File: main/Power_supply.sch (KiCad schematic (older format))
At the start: 39 parts, among them IC1 TPS54294PWP, IC2 TPS54294PWP, J3 Barrel_Jack

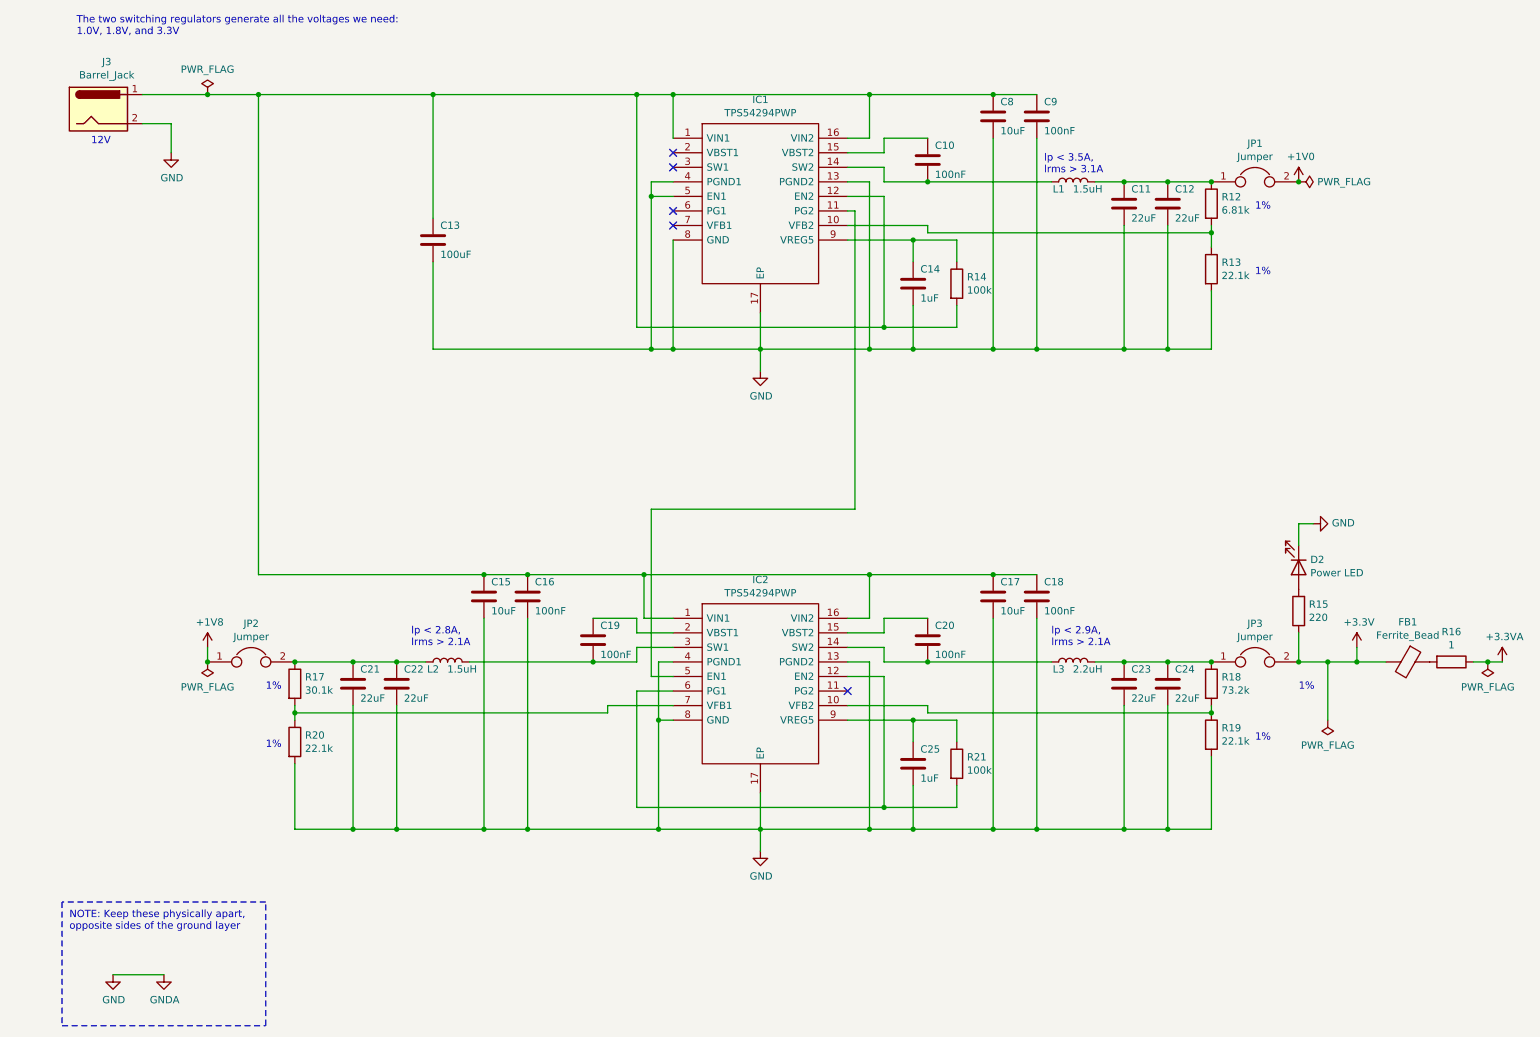
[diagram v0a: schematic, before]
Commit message: DAC: Remove amplifier, replace with low pass as per datasheet
Also: a lot of footprint association
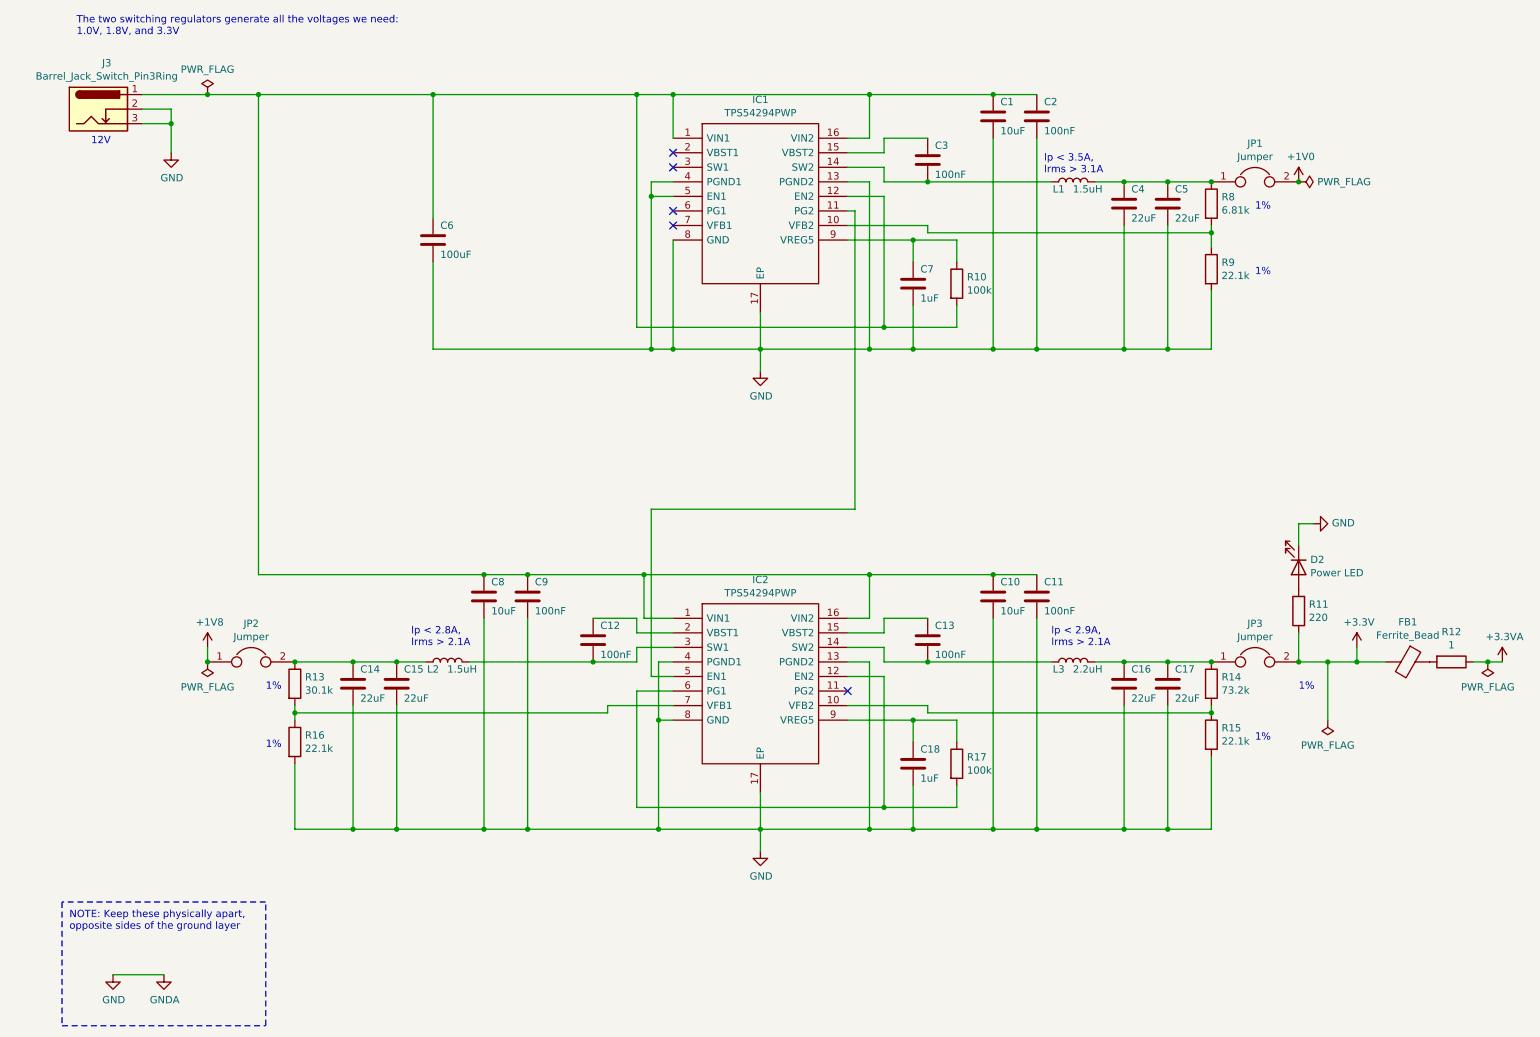
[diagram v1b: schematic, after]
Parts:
- removed J3: Barrel_Jack, symbol Connector:Barrel_Jack
- added J3: Barrel_Jack_Switch_Pin3Ring, Connector_BarrelJack:BarrelJack_CUI_PJ-102AH_Horizontal, symbol Connector:Barrel_Jack_Switch_Pin3Ring
- C1: renamed from C8; footprint (none) -> Capacitor_SMD:C_0805_2012Metric_Pad1.18x1.45mm_HandSolder
- C10: renamed from C17; footprint (none) -> Capacitor_SMD:C_0805_2012Metric_Pad1.18x1.45mm_HandSolder
- C11: renamed from C18; footprint (none) -> Capacitor_SMD:C_0805_2012Metric_Pad1.18x1.45mm_HandSolder
- C12: renamed from C19; footprint (none) -> Capacitor_SMD:C_0805_2012Metric_Pad1.18x1.45mm_HandSolder
- C13: renamed from C20; footprint (none) -> Capacitor_SMD:C_0805_2012Metric_Pad1.18x1.45mm_HandSolder
- C14: renamed from C21; footprint (none) -> Capacitor_SMD:C_0805_2012Metric_Pad1.18x1.45mm_HandSolder
- C15: renamed from C22; footprint (none) -> Capacitor_SMD:C_0805_2012Metric_Pad1.18x1.45mm_HandSolder
- C16: renamed from C23; footprint (none) -> Capacitor_SMD:C_0805_2012Metric_Pad1.18x1.45mm_HandSolder
- C17: renamed from C24; footprint (none) -> Capacitor_SMD:C_0805_2012Metric_Pad1.18x1.45mm_HandSolder
- C18: renamed from C25; footprint (none) -> Capacitor_SMD:C_0805_2012Metric_Pad1.18x1.45mm_HandSolder
- C2: renamed from C9; footprint (none) -> Capacitor_SMD:C_0805_2012Metric_Pad1.18x1.45mm_HandSolder
- C3: renamed from C10; footprint (none) -> Capacitor_SMD:C_0805_2012Metric_Pad1.18x1.45mm_HandSolder
- C4: renamed from C11; footprint (none) -> Capacitor_SMD:C_0805_2012Metric_Pad1.18x1.45mm_HandSolder
- C5: renamed from C12; footprint (none) -> Capacitor_SMD:C_0805_2012Metric_Pad1.18x1.45mm_HandSolder
- C7: renamed from C14; footprint (none) -> Capacitor_SMD:C_0805_2012Metric_Pad1.18x1.45mm_HandSolder
- C8: renamed from C15; footprint (none) -> Capacitor_SMD:C_0805_2012Metric_Pad1.18x1.45mm_HandSolder
- C9: renamed from C16; footprint (none) -> Capacitor_SMD:C_0805_2012Metric_Pad1.18x1.45mm_HandSolder
- FB1: footprint (none) -> Resistor_SMD:R_0805_2012Metric_Pad1.20x1.40mm_HandSolder
- JP1, JP2, JP3: footprint (none) -> Connector_PinHeader_2.54mm:PinHeader_2x01_P2.54mm_Vertical
- renumbered C13 to C6, R14 to R10, R15 to R11, R16 to R12, R17 to R13, R18 to R14, R19 to R15, R20 to R16, R21 to R17, R12 to R8, R13 to R9
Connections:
- net GND: now also J3.2, J3.3
- net at C1.1, C10.1, C11.1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: now also J3.1

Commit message: Start PCB layout
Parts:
- D2: Manufacturer_Name (none) -> Wurth Electronic; Manufacturer_Part_Number (none) -> 150080RS75000; URL (none) -> https://no.farnell.com/wurth-elektronik/150080rs75000/led-0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
- FB1: Manufacturer_Name (none) -> TE; Manufacturer_Part_Number (none) -> BMB2A0060LN2; URL (none) -> https://no.farnell.com/sigmainductors-te-connectivity/bmb2a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
- IC1, IC2: URL (none) -> https://no.farnell.com/texas-instruments/tps54294pwp/buck-s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
- J3: Manufacturer_Name (none) -> CUI Devices; Manufacturer_Part_Number (none) -> PJ-002A; URL (none) -> https://www.digikey.no/product-detail/no/cui-devices/PJ-002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
- L1, L2: Manufacturer_Name (none) -> muRata; Manufacturer_Part_Number (none) -> 1286AS-H-2R2M=P2; URL (none) -> https://no.farnell.com/murata/1286as-h-2r2m-p2/inductor-2-2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
- L3: Manufacturer_Name (none) -> muRata; Manufacturer_Part_Number (none) -> DFE201610E-1R5M=P2; URL (none) -> https://no.farnell.com/murata/dfe201610e-1r5m-p2/inductor-1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
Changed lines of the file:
@@
 F 10 "TPS54294PWP" H 5900 4200 50  0001 L CNN "Arrow Part Number"
 F 11 "https://www.arrow.com/en/products/tps54294pwp/texas-instruments" H 5900 4100 50  0001 L CNN "Arrow Price/Stock"
+F 12 "https://no.farnell.com/texas-instruments/tps54294pwp/buck-sync-adj-2a-dl-16htssop/dp/3008251" H 4850 4900 50  0001 C CNN "URL"
 	1    4850 4900
 	1    0    0    -1
@@
 F 1 "1.5uH" V 3250 5100 50  0000 C CNN
 F 2 "Inductor_SMD:L_1806_4516Metric_Pad1.57x1.80mm_HandSolder" H 3300 5200 50  0001 C CNN
-F 3 "~" H 3300 5200 50  0001 C CNN
+F 3 "https://www.farnell.com/datasheets/2021974.pdf" H 3300 5200 50  0001 C CNN
+F 4 "muRata" H 3300 5200 50  0001 C CNN "Manufacturer_Name"
+F 5 "1286AS-H-2R2M=P2" H 3300 5200 50  0001 C CNN "Manufacturer_Part_Number"
+F 6 "https://no.farnell.com/murata/1286as-h-2r2m-p2/inductor-2-2uh-20-1-5a-shld-0806/dp/2530046?st=inductor%20smd%200806" H 3300 5200 50  0001 C CNN "URL"
 	1    3300 5200
 	0    -1   -1   0
@@
 F 1 "2.2uH" V 7550 5100 50  0000 C CNN
 F 2 "Inductor_SMD:L_1806_4516Metric_Pad1.57x1.80mm_HandSolder" H 7600 5200 50  0001 C CNN
-F 3 "~" H 7600 5200 50  0001 C CNN
+F 3 "https://www.farnell.com/datasheets/2339713.pdf" H 7600 5200 50  0001 C CNN
+F 4 "muRata" H 7600 5200 50  0001 C CNN "Manufacturer_Name"
+F 5 "DFE201610E-1R5M=P2" H 7600 5200 50  0001 C CNN "Manufacturer_Part_Number"
+F 6 "https://no.farnell.com/murata/dfe201610e-1r5m-p2/inductor-1-5uh-2-4a-0806-shielded/dp/2776797?st=inductor%20smd%200806" H 7600 5200 50  0001 C CNN "URL"
 	1    7600 5200
 	0    -1   -1   0
@@
 F 1 "Ferrite_Bead" V 9717 5200 50  0000 C CNN
 F 2 "Resistor_SMD:R_0805_2012Metric_Pad1.20x1.40mm_HandSolder" V 9830 5200 50  0001 C CNN
-F 3 "~" H 9900 5200 50  0001 C CNN
+F 3 "https://www.farnell.com/datasheets/38013.pdf" H 9900 5200 50  0001 C CNN
+F 4 "TE" H 9900 5200 50  0001 C CNN "Manufacturer_Name"
+F 5 "BMB2A0060LN2" H 9900 5200 50  0001 C CNN "Manufacturer_Part_Number"
+F 6 "https://no.farnell.com/sigmainductors-te-connectivity/bmb2a0060ln2/ferrite-bead-0-05ohm-850ma-0805/dp/1193419?st=ferrite%20bead%200805" H 9900 5200 50  0001 C CNN "URL"
 	1    9900 5200
 	0    1    1    0
@@
 F 10 "TPS54294PWP" H 5900 900 50  0001 L CNN "Arrow Part Number"
 F 11 "https://www.arrow.com/en/products/tps54294pwp/texas-instruments" H 5900 800 50  0001 L CNN "Arrow Price/Stock"
+F 12 "https://no.farnell.com/texas-instruments/tps54294pwp/buck-sync-adj-2a-dl-16htssop/dp/3008251" H 4850 1600 50  0001 C CNN "URL"
 	1    4850 1600
 	1    0    0    -1
@@
 F 1 "1.5uH" V 7550 1800 50  0000 C CNN
 F 2 "Inductor_SMD:L_1806_4516Metric_Pad1.57x1.80mm_HandSolder" H 7600 1900 50  0001 C CNN
-F 3 "~" H 7600 1900 50  0001 C CNN
+F 3 "https://www.farnell.com/datasheets/2021974.pdf" H 7600 1900 50  0001 C CNN
+F 4 "muRata" H 7600 1900 50  0001 C CNN "Manufacturer_Name"
+F 5 "1286AS-H-2R2M=P2" H 7600 1900 50  0001 C CNN "Manufacturer_Part_Number"
+F 6 "https://no.farnell.com/murata/1286as-h-2r2m-p2/inductor-2-2uh-20-1-5a-shld-0806/dp/2530046?st=inductor%20smd%200806" H 7600 1900 50  0001 C CNN "URL"
 	1    7600 1900
 	0    -1   -1   0
@@
 F 1 "Power LED" V 9188 4630 50  0000 L CNN
 F 2 "LED_SMD:LED_0805_2012Metric_Pad1.15x1.40mm_HandSolder" H 9150 4550 50  0001 C CNN
-F 3 "~" H 9150 4550 50  0001 C CNN
+F 3 "https://www.farnell.com/datasheets/1911350.pdf" H 9150 4550 50  0001 C CNN
+F 4 "Wurth Electronic" H 9150 4550 50  0001 C CNN "Manufacturer_Name"
+F 5 "150080RS75000" H 9150 4550 50  0001 C CNN "Manufacturer_Part_Number"
+F 6 "https://no.farnell.com/wurth-elektronik/150080rs75000/led-0805-red-150mcd-625nm/dp/2322077?st=0805%20led" H 9150 4550 50  0001 C CNN "URL"
 	1    9150 4550
 	0    1    1    0
@@
 F 1 "Barrel_Jack_Switch_Pin3Ring" H 957 1626 50  0000 C CNN
 F 2 "Connector_BarrelJack:BarrelJack_CUI_PJ-102AH_Horizontal" H 950 1360 50  0001 C CNN
-F 3 "~" H 950 1360 50  0001 C CNN
+F 3 "https://www.cuidevices.com/product/resource/digikeypdf/pj-002a.pdf~" H 950 1360 50  0001 C CNN
+F 4 "CUI Devices" H 900 1400 50  0001 C CNN "Manufacturer_Name"
+F 5 " PJ-002A " H 900 1400 50  0001 C CNN "Manufacturer_Part_Number"
+F 6 "https://www.digikey.no/product-detail/no/cui-devices/PJ-002A/CP-002A-ND/96962" H 900 1400 50  0001 C CNN "URL"
 	1    900  1400
 	1    0    0    -1

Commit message: Continue PCB layout
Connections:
- net +1V8: now also JP2.2; no longer JP2.1
- net at C14.1, C15.1, L2.1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: now also JP2.1; no longer JP2.2
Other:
- moved on the sheet: JP2
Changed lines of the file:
@@
 U 1 1 6165E780
 P 1950 5200
-F 0 "JP2" H 1950 5464 50  0000 C CNN
-F 1 "Jumper" H 1950 5373 50  0000 C CNN
+F 0 "JP2" H 1950 5100 50  0000 C CNN
+F 1 "Jumper" H 1950 5000 50  0000 C CNN
 F 2 "Connector_PinHeader_2.54mm:PinHeader_2x01_P2.54mm_Vertical" H 1950 5200 50  0001 C CNN
 F 3 "~" H 1950 5200 50  0001 C CNN
 	1    1950 5200
-	1    0    0    -1
+	-1   0    0    1
 $EndComp
 Connection ~ 1650 5200

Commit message: Some more routing
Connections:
- net at C12.2, IC2.3 (SW1): now also L2.1; no longer L2.2
- net at C14.1, C15.1, JP2.1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: now also L2.2; no longer L2.1
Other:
- moved on the sheet: L2
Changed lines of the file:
@@
 F 6 "https://no.farnell.com/murata/1286as-h-2r2m-p2/inductor-2-2uh-20-1-5a-shld-0806/dp/2530046?st=inductor%20smd%200806" H 3300 5200 50  0001 C CNN "URL"
 	1    3300 5200
-	0    -1   -1   0
+	0    1    1    0
 $EndComp
 $Comp

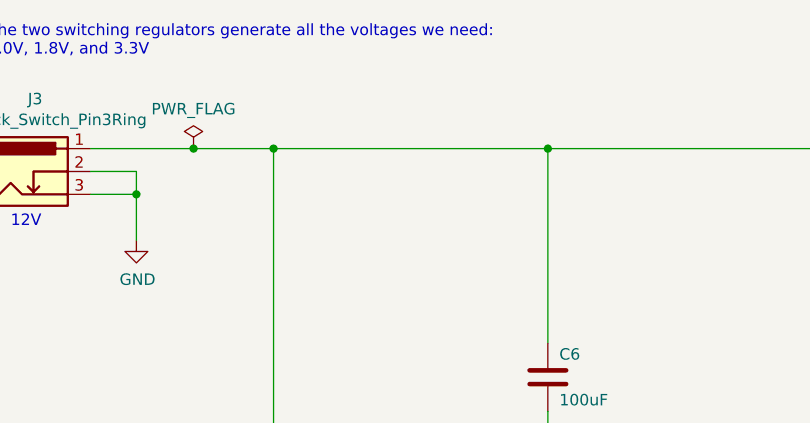
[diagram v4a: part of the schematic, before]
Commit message: Almost finished with PCB layout
- Fixed FPGA power layout. The 1V0, 1V8 and 3V3 pins have to be
  connected to vias which in turn connect to fat lanes

- Added logo and names

- Started power circuit, this needs some work
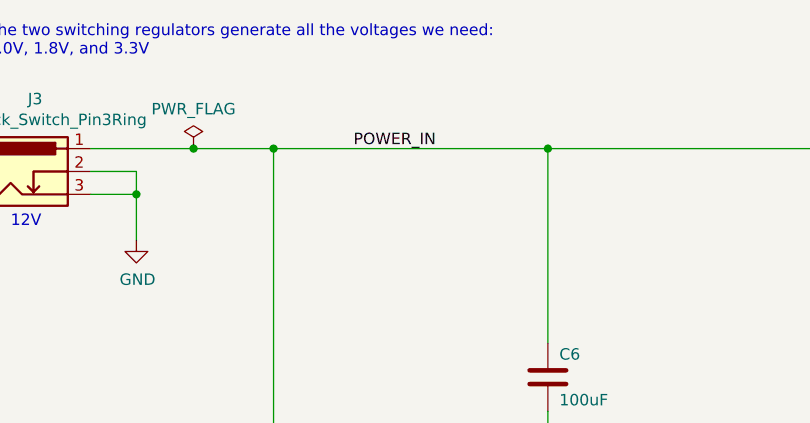
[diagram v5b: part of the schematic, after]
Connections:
- net POWER_IN: now reaches C1.1, C10.1, C11.1, C2.1, C6.1, C8.1, C9.1, IC1.1 (VIN1), IC1.12 (EN2), IC1.16 (VIN2), IC2.1 (VIN1), IC2.16 (VIN2), J3.1, R10.2
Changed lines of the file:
@@
 	1400 1400 1400 1500
 Connection ~ 1400 1500
+Text Label 2350 1300 0    50   ~ 0
+POWER_IN
 $EndSCHEMATC

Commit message: Add missing resistor to power supply
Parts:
- added R46: 100k, Resistor_SMD:R_0805_2012Metric_Pad1.20x1.40mm_HandSolder, symbol Device:R
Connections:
- net at IC1.11 (PG2), IC2.5 (EN1): now also R46.2
- net at IC1.10 (VFB2), R8.2, R9.1: now also R10.1, R46.1
- net at C7.1, IC1.9 (VREG5): no longer R10.1
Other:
- note added: "Missing from v1.0.0\n"
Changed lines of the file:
@@
 	6500 2450 6500 2300
-Wire Wire Line
-	6800 2450 6800 2300
 Wire Wire Line
 	4600 2900 6300 2900
@@
 Connection ~ 8250 1900
 Wire Wire Line
-	8550 2250 6600 2250
+	8550 2250 6800 2250
 Wire Wire Line
 	6600 2250 6600 2200
@@
 Text Label 2350 1300 0    50   ~ 0
 POWER_IN
+$Comp
+L Device:R R46
+U 1 1 61A799C5
+P 6550 2100
+F 0 "R46" V 6450 2200 50  0000 L CNN
+F 1 "100k" V 6450 1950 50  0000 L CNN
+F 2 "Resistor_SMD:R_0805_2012Metric_Pad1.20x1.40mm_HandSolder" V 6480 2100 50  0001 C CNN
+F 3 "~" H 6550 2100 50  0001 C CNN
+	1    6550 2100
+	0    1    1    0
+$EndComp
+Wire Wire Line
+	6800 2250 6800 2450
+Wire Wire Line
+	6800 2250 6800 2100
+Wire Wire Line
+	6700 2100 6800 2100
+Connection ~ 6800 2250
+Wire Wire Line
+	6800 2250 6600 2250
+Wire Wire Line
+	6400 2100 6100 2100
+Connection ~ 6100 2100
+Text Notes 6700 2150 0    50   ~ 0
+Missing from v1.0.0\n
+Wire Notes Line
+	6400 1950 6400 2150
+Wire Notes Line
+	6400 2150 7450 2150
+Wire Notes Line
+	7450 2150 7450 1950
+Wire Notes Line
+	7450 1950 6400 1950
 $EndSCHEMATC
